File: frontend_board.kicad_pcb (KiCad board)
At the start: 4 copper layers, 72.5 x 50 mm, 127 parts, among them J1 Conn_02x20_Odd_Even, J2 Conn_02x10_Odd_Even, J3 Conn_02x20_Odd_Even, U1 ADS1299_TQFP, U2 ADM7170, U3 LD1117S50TR_SOT223

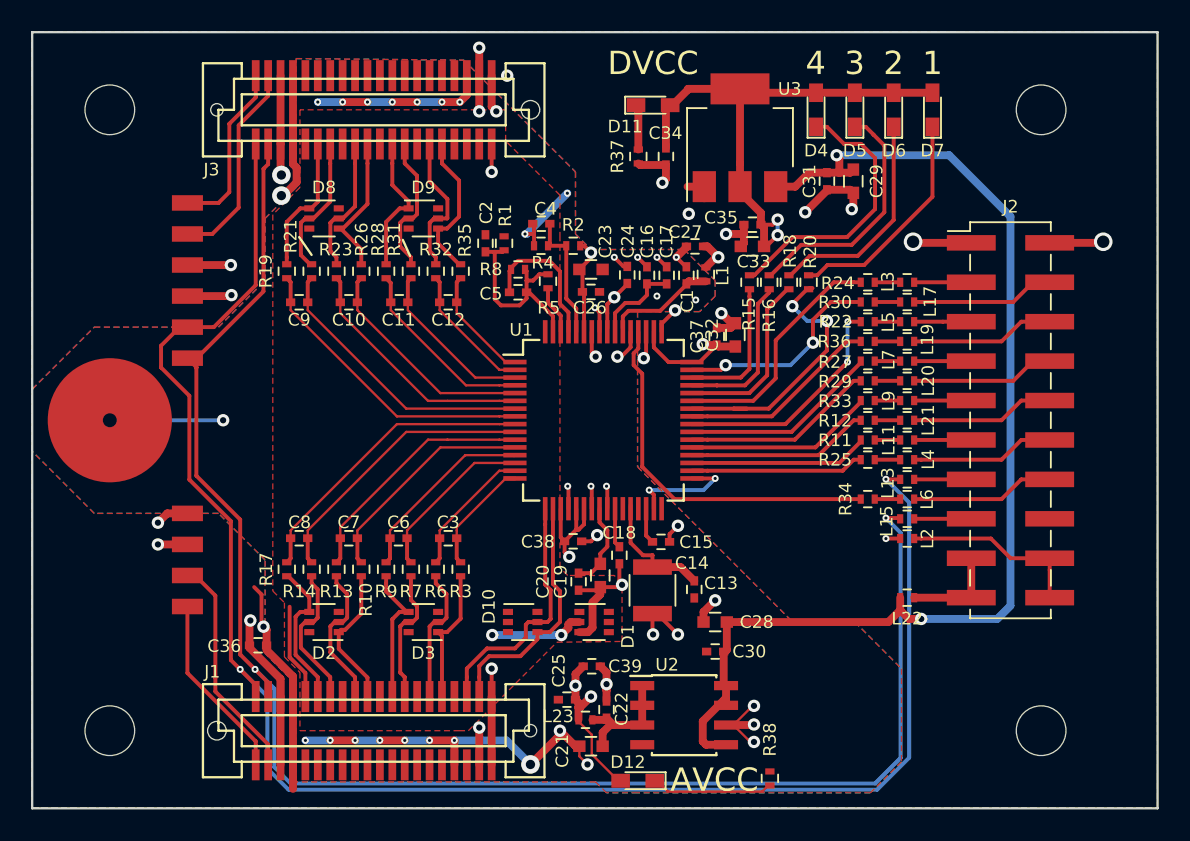
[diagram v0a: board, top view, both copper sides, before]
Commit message: frontend: Reshape to 60x70mm, fixup silk
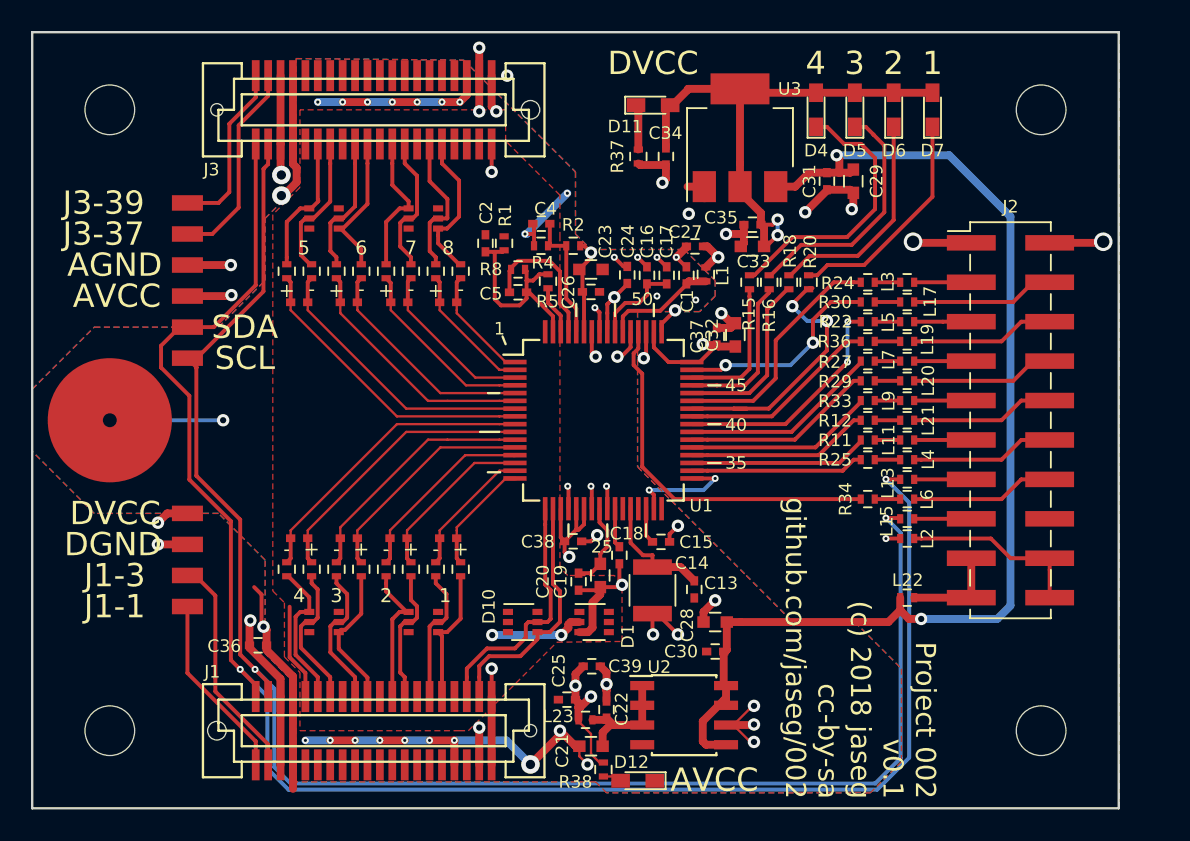
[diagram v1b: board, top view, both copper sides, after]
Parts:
- C10, C11, C12, C3, C6, C7, C8, C9: footprint Capacitors_SMD:C_0402 -> Capacitors_SMD:C_0402_NoSilk
- D2, D3, D8, D9: footprint TO_SOT_Packages_SMD:SOT-363_SC-70-6 -> footprints:SOT-363_SC-70-6-nosilk
- moved R38 10.7 mm to (146.8, 137.5), turned to 90 degrees
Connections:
- D12 pad 1: Net-(D12-Pad1) -> VSSA
- D12 pad 2: VDDA -> Net-(D12-Pad2)
- R38 pad 1: VSSA -> Net-(D12-Pad2)
- R38 pad 2: Net-(D12-Pad1) -> VDDA
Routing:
- net Net-(D12-Pad1): track 7.87 -> 0.00 mm
- net VDDA: track 48.7 -> 47.1 mm
- net Net-(D12-Pad2): track 0.00 -> 1.37 mm
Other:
- board size 72.5 x 50 mm -> 70 x 50 mm
- net class Default: clearance 0.127 -> 0.089; trace_width 0.127 -> 0.089
- rule trace_clearance: 0.127 -> 0.089
- rule trace_min: 0.127 -> 0.089
- board text added: "+"
- board text added: "-"
- board text added: "25"
- board text added: "35"
- board text added: "40"
- board text added: "45"
- board text added: "5"
- board text added: "50"
- board text added: "6"
- board text added: "7"
- board text added: "8"
- board text added: "AGND"
- board text added: "DGND"
- board text added: "J1-1"
- board text added: "J1-3"
- board text added: "J3-37"
- board text added: "J3-39"
- board text added: "Project 002 v0.1 (c) 2018 jaseg cc-by-sa github.com/jaseg/002"
- board text added: "SCL"
- board text added: "SDA"
